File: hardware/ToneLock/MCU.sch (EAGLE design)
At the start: 4 parts, among them U1 LD1117S33TR

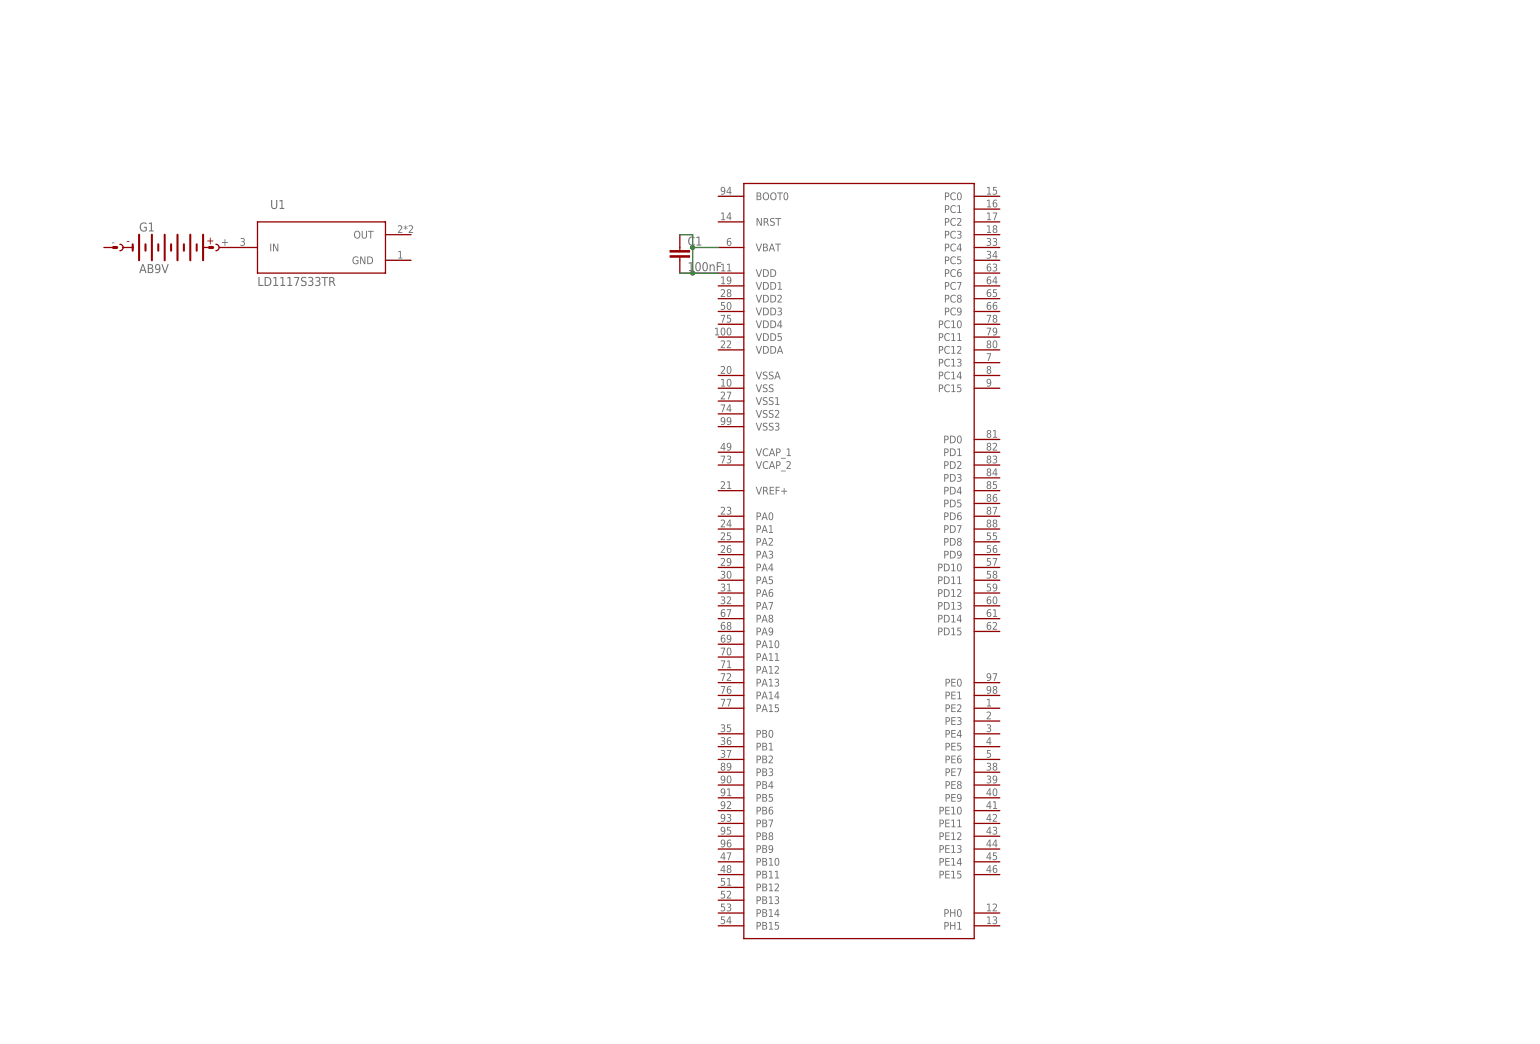
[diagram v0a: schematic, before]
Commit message: Added accelerometer, microphone into schematic and added libraries
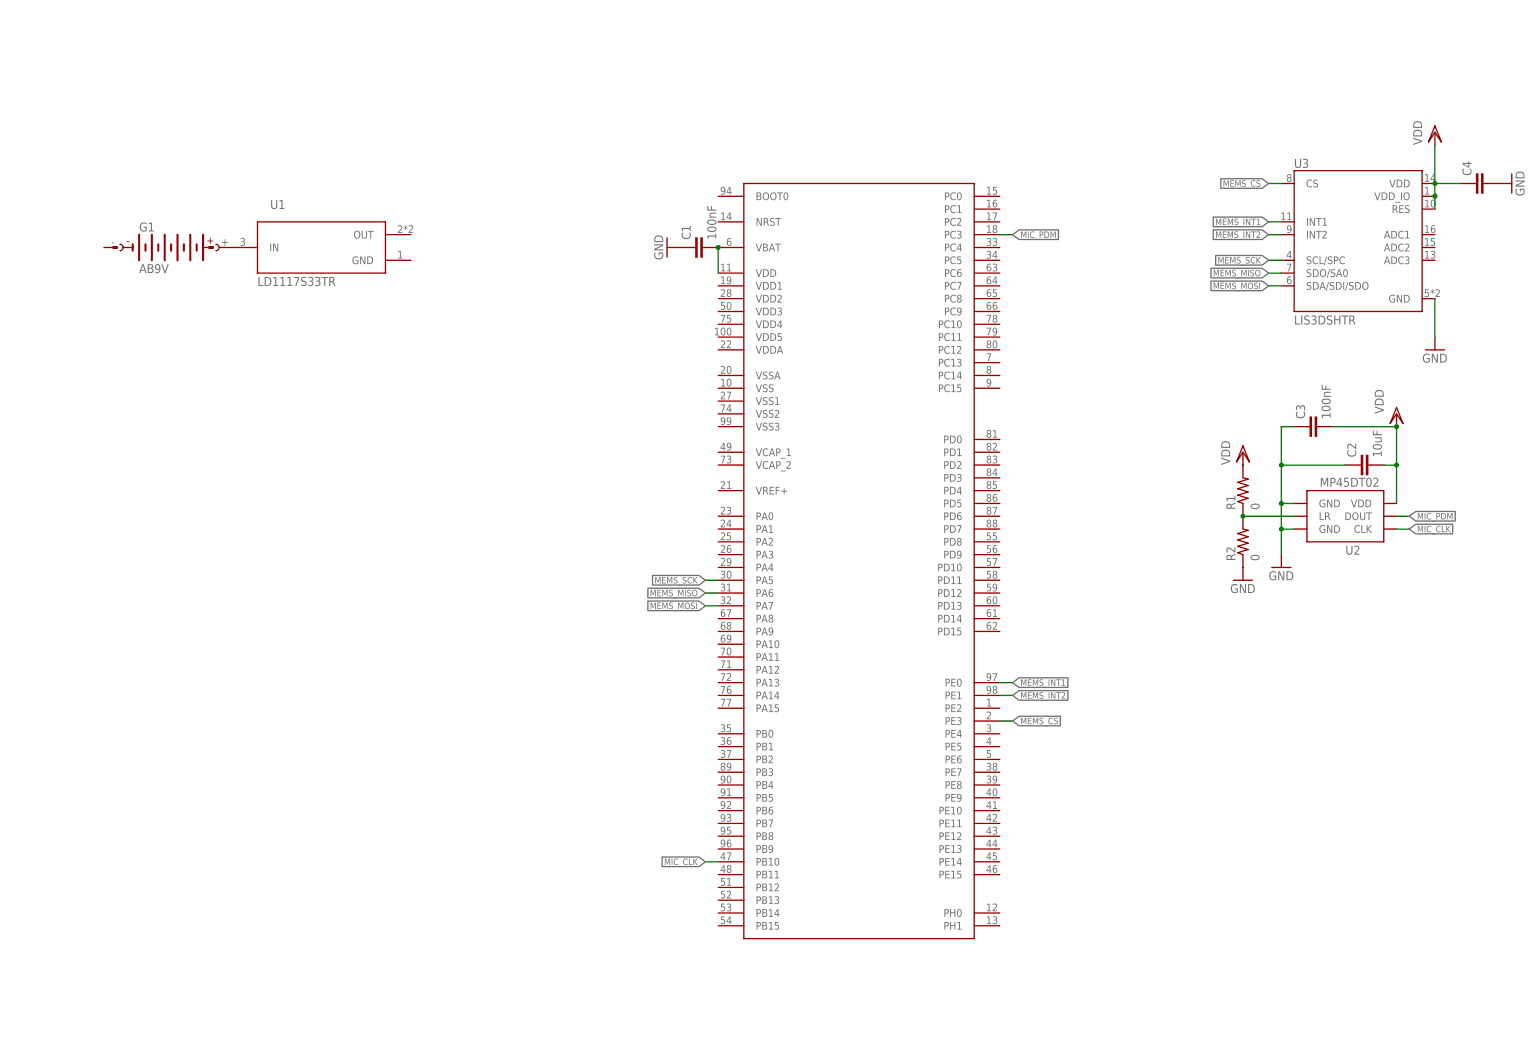
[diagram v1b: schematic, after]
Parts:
- added C2: 10uF, resistor:C-EUC0805
- added C3: 100nF, resistor:C-EUC0603
- added C4: (no value), resistor:C-EUC0603
- added R1, R2: 0, resistor:R-US_R0603
- added U2: MP45DT02, MP45DT02:MP45DT02
- added U3: LIS3DSHTR, LIS3DSHTR:LIS3DSHTR
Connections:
- new net GND: C1.1, C2.1, C3.1, C4.2, R2.1, U2.GND@1, U2.GND@2, U3.GND
- new net MEMS_CS: U$1.PE3, U3.CS
- new net MEMS_INT1: U$1.PE0, U3.INT1
- new net MEMS_INT2: U$1.PE1, U3.INT2
- new net MEMS_MISO: U$1.PA6, U3.SDO/SA0
- new net MEMS_MOSI: U$1.PA7, U3.SDA/SDI/SDO
- new net MEMS_SCK: U$1.PA5, U3.SCL/SPC
- new net MIC_CLK: U$1.PB10, U2.CLK
- new net MIC_PDM: U$1.PC3, U2.DOUT
- new net N$3: R1.1, R2.2, U2.LR
- new net VDD: C2.2, C3.2, C4.1, R1.2, U2.VDD, U3.RES, U3.VDD, U3.VDD_IO
- net N$1: no longer C1.1
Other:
- moved on the sheet: C1

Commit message: Renamed datasheets and Added UART pins
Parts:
- added C5: 10uF, resistor:C-EUC0805
- added JP1: (no value), pinhead:PINHD-1X2
- C4: value (none) -> 100nF
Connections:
- new net UART4_RX: JP1.1, U$1.PA1
- new net UART4_TX: JP1.2, U$1.PA0
- net GND: now also C5.2
- net VDD: now also C5.1
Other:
- moved on the sheet: C2, C3, C4, R1, R2, U2, U3

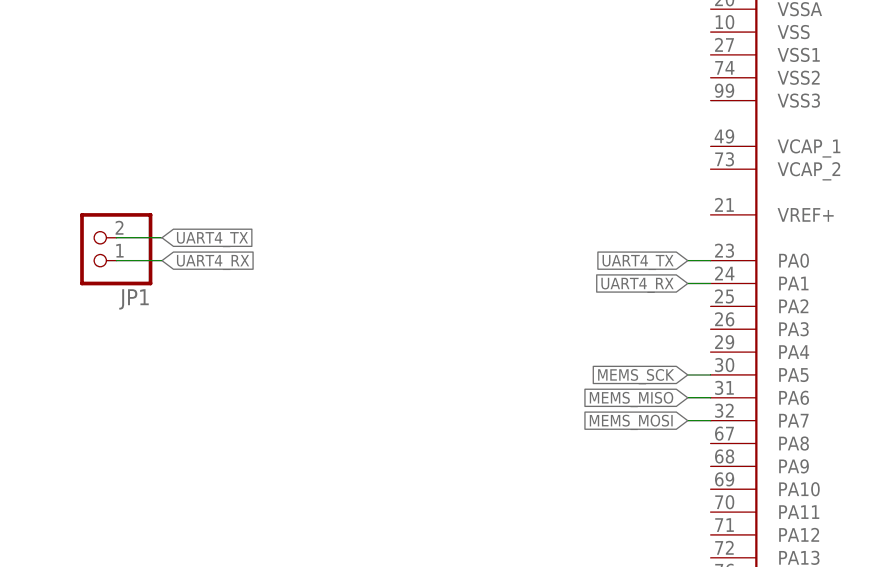
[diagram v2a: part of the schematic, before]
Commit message: Changed UART to use USART2
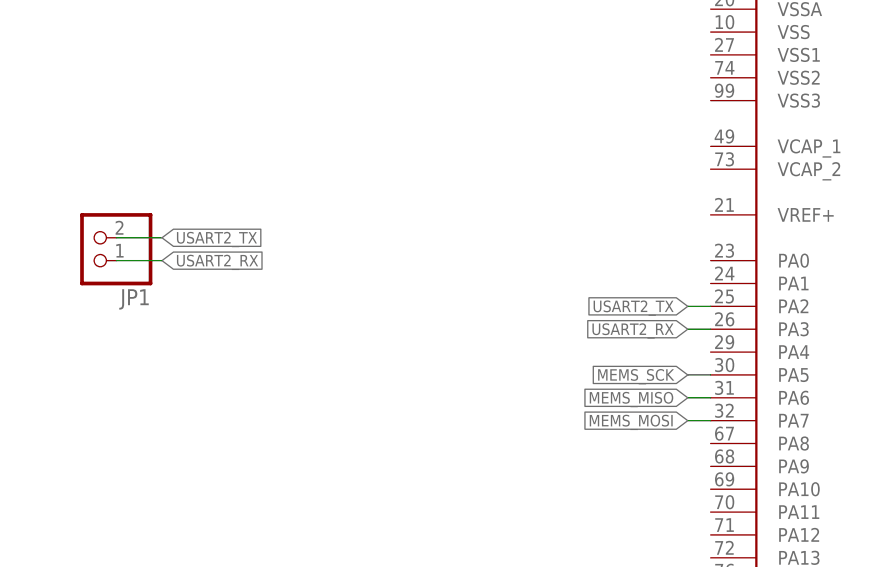
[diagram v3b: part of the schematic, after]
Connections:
- removed net UART4_RX: JP1.1, U$1.PA1
- removed net UART4_TX: JP1.2, U$1.PA0
- new net USART2_RX: JP1.1, U$1.PA3
- new net USART2_TX: JP1.2, U$1.PA2
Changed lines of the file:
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@@
 </segment>
 </net>
-<net name="UART4_TX" class="0">
+<net name="USART2_RX" class="0">
 <segment>
-<pinref part="U$1" gate="G$1" pin="PA0"/>
-<wire x1="-5.08" y1="83.82" x2="-7.62" y2="83.82" width="0.1524" layer="91"/>
-<label x="-7.62" y="83.82" size="1.27" layer="95" rot="R180" xref="yes"/>
+<pinref part="JP1" gate="G$1" pin="1"/>
+<wire x1="-71.12" y1="83.82" x2="-66.04" y2="83.82" width="0.1524" layer="91"/>
+<label x="-66.04" y="83.82" size="1.27" layer="95" xref="yes"/>
 </segment>
+<segment>
+<pinref part="U$1" gate="G$1" pin="PA3"/>
+<wire x1="-5.08" y1="76.2" x2="-7.62" y2="76.2" width="0.1524" layer="91"/>
+<label x="-7.62" y="76.2" size="1.27" layer="95" rot="R180" xref="yes"/>
+</segment>
+</net>
+<net name="USART2_TX" class="0">
 <segment>
 <pinref part="JP1" gate="G$1" pin="2"/>
@@
 <label x="-66.04" y="86.36" size="1.27" layer="95" xref="yes"/>
 </segment>
-</net>
-<net name="UART4_RX" class="0">
 <segment>
-<pinref part="U$1" gate="G$1" pin="PA1"/>
-<wire x1="-5.08" y1="81.28" x2="-7.62" y2="81.28" width="0.1524" layer="91"/>
-<label x="-7.62" y="81.28" size="1.27" layer="95" rot="R180" xref="yes"/>
-</segment>
-<segment>
-<pinref part="JP1" gate="G$1" pin="1"/>
-<wire x1="-71.12" y1="83.82" x2="-66.04" y2="83.82" width="0.1524" layer="91"/>
-<label x="-66.04" y="83.82" size="1.27" layer="95" xref="yes"/>
+<pinref part="U$1" gate="G$1" pin="PA2"/>
+<wire x1="-5.08" y1="78.74" x2="-7.62" y2="78.74" width="0.1524" layer="91"/>
+<label x="-7.62" y="78.74" size="1.27" layer="95" rot="R180" xref="yes"/>
 </segment>
 </net>

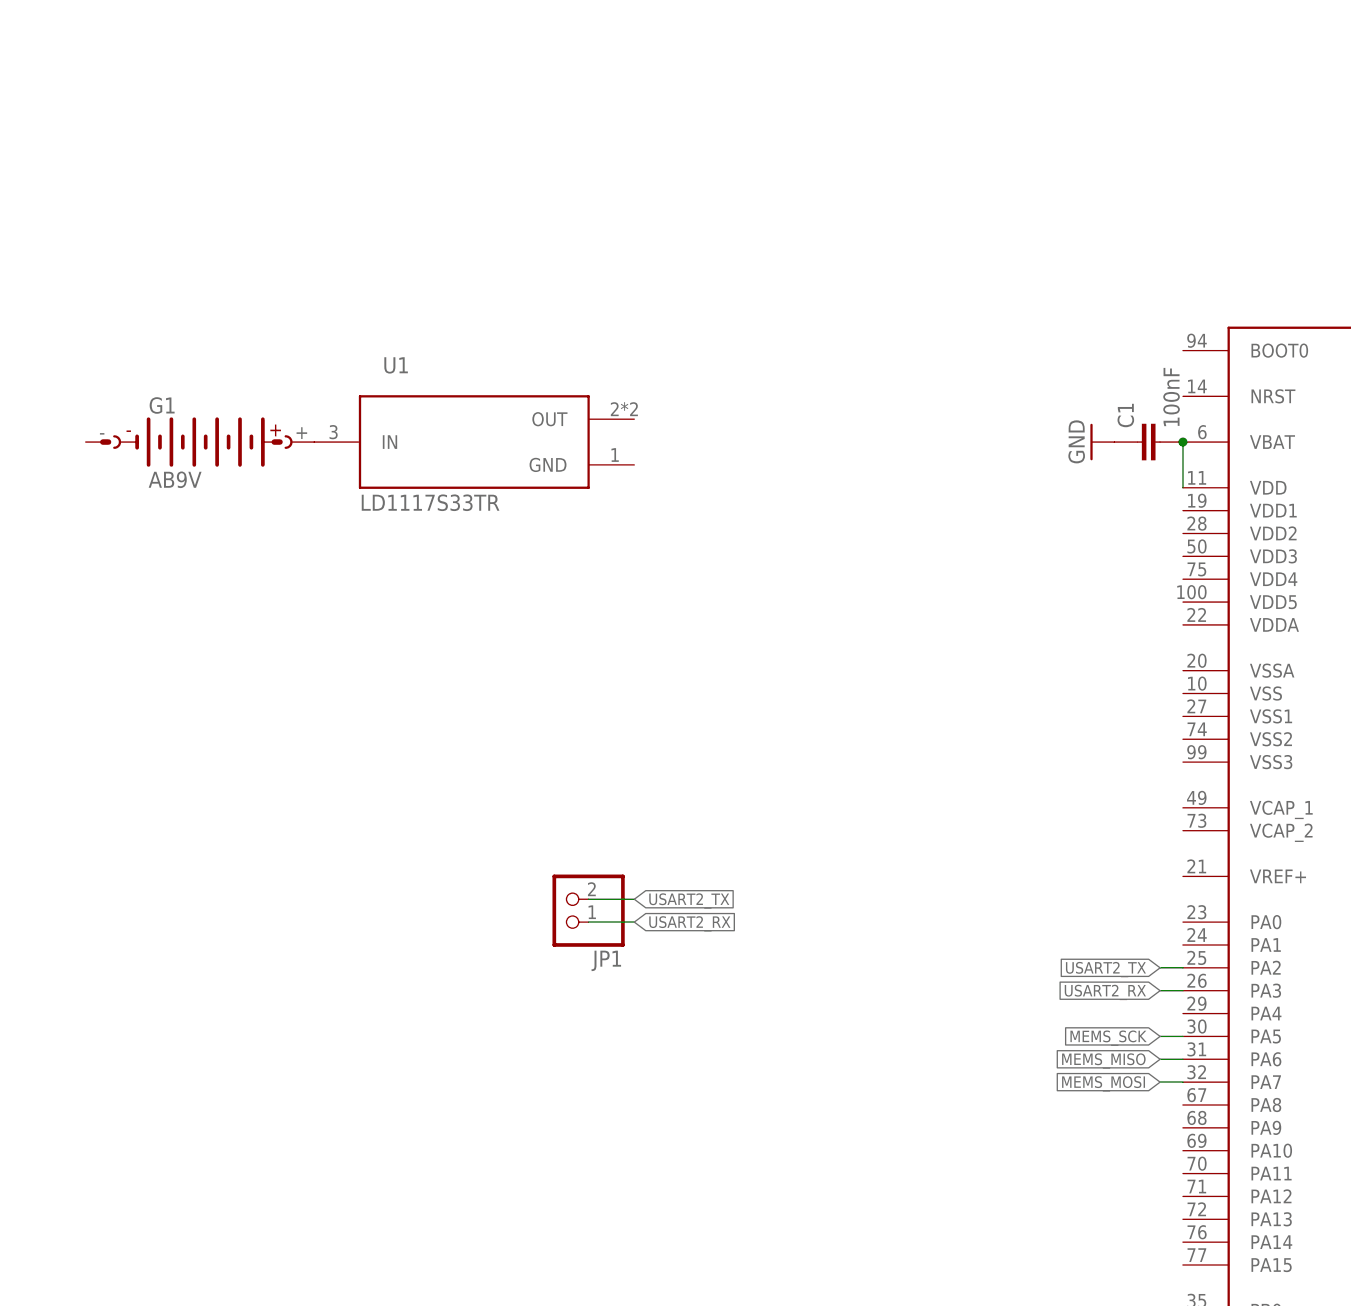
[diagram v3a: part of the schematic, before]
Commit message: Changed VCC header
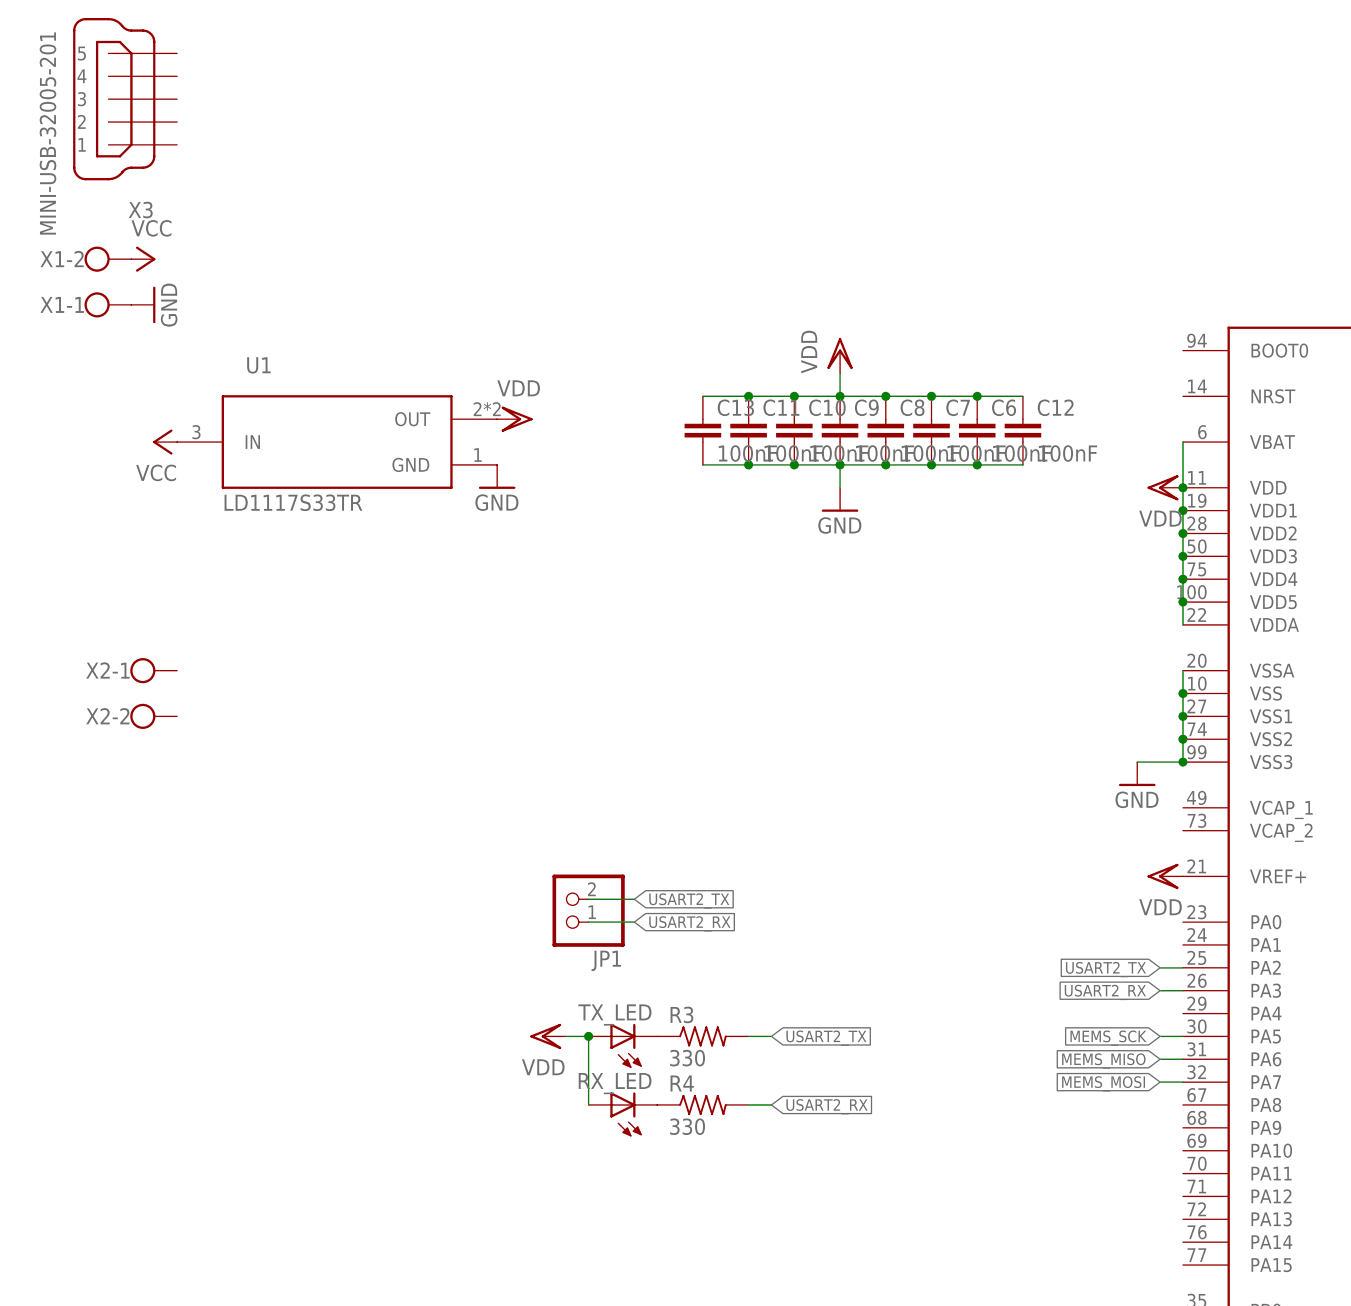
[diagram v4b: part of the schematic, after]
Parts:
- removed C1: 100nF, resistor:C-EUC0603
- removed G1: AB9V, battery:AB9V
- added C10, C11, C12, C13, C6, C7, C8, C9: 100nF, resistor:C-EUC0603
- added R3, R4: 330, resistor:R-US_R0603
- added RX_LED, TX_LED: (no value), led:LEDCHIP-LED0603
- added X1, X2: (no value), con-wago-500:W237-102
- added X3: MINI-USB-32005-201, con-cypressindustries:MINI-USB-32005-201
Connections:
- removed net N$2: G1.+, U1.IN
- new net N$4: R4.1, RX_LED.C
- new net VCC: U1.IN, X1-2.KL
- net GND: now also C10.2, C11.2, C12.2, C13.2, C6.2, C7.2, C8.2, C9.2, U$1.VSS, U$1.VSS1, U$1.VSS2, U$1.VSS3, U$1.VSSA, U1.GND, X1-1.KL; no longer C1.1
- net N$1: now also R3.1, TX_LED.C; no longer C1.2, U$1.VBAT, U$1.VDD
- net USART2_RX: now also R4.2
- net USART2_TX: now also R3.2
- net VDD: now also C10.1, C11.1, C12.1, C13.1, C6.1, C7.1, C8.1, C9.1, RX_LED.A, TX_LED.A, U$1.VBAT, U$1.VDD, U$1.VDD1, U$1.VDD2, U$1.VDD3, U$1.VDD4, U$1.VDD5, U$1.VDDA, U$1.VREF+, U1.OUT
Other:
- moved on the sheet: U1
